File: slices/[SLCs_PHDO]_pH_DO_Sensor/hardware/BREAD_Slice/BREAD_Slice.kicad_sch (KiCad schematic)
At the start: 1 part, among them J8 Conn_01x10_Female

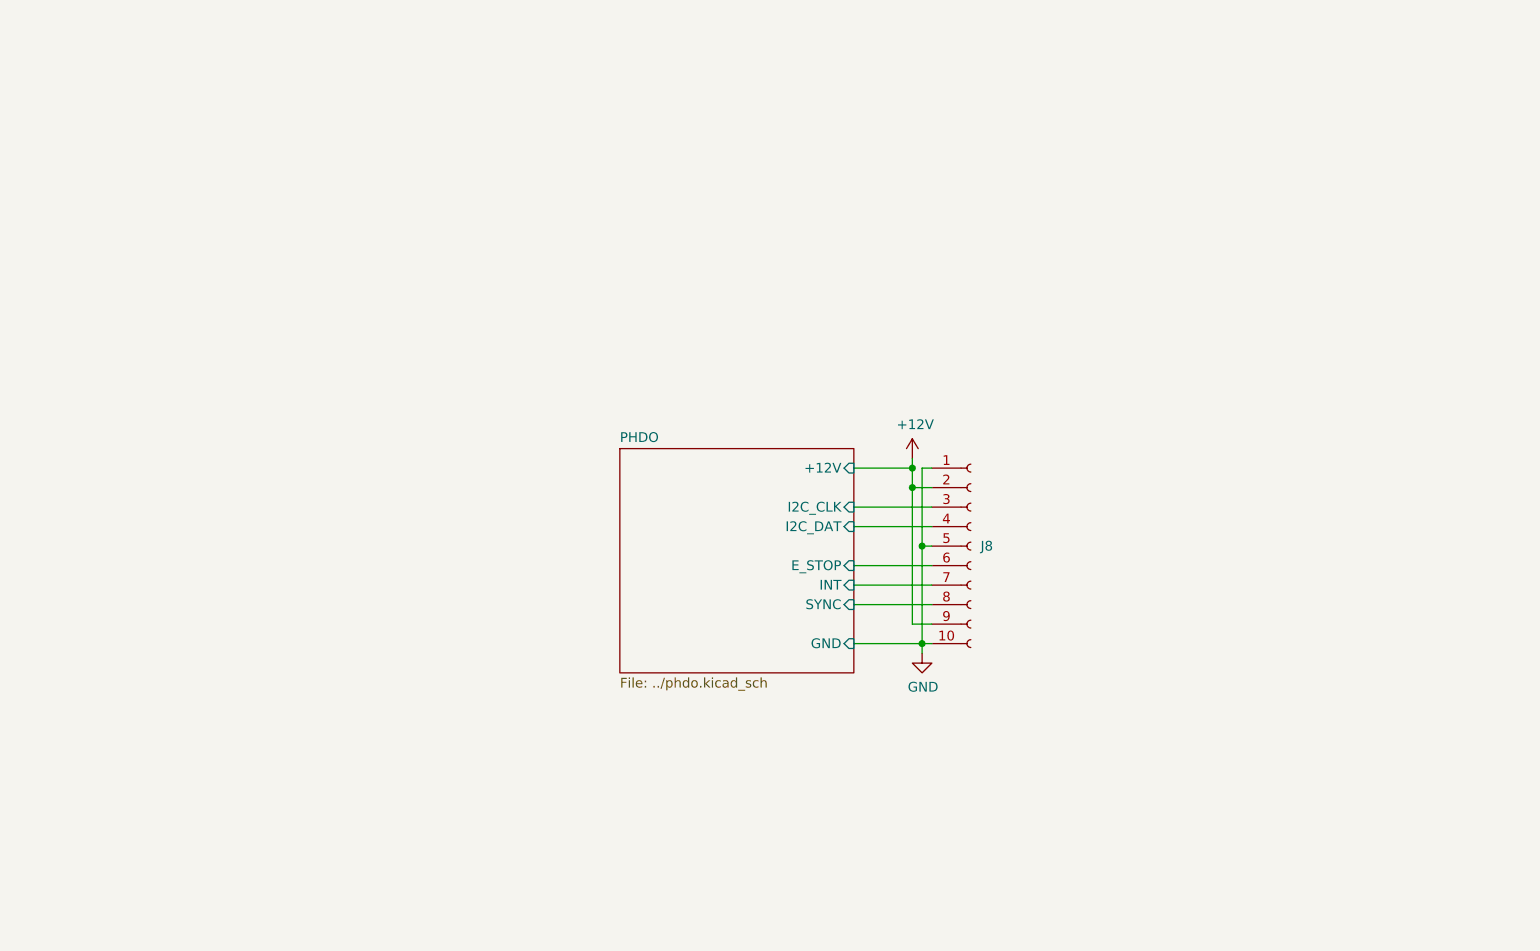
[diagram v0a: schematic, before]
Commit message: improved phdo and initial ERC pass on PDER
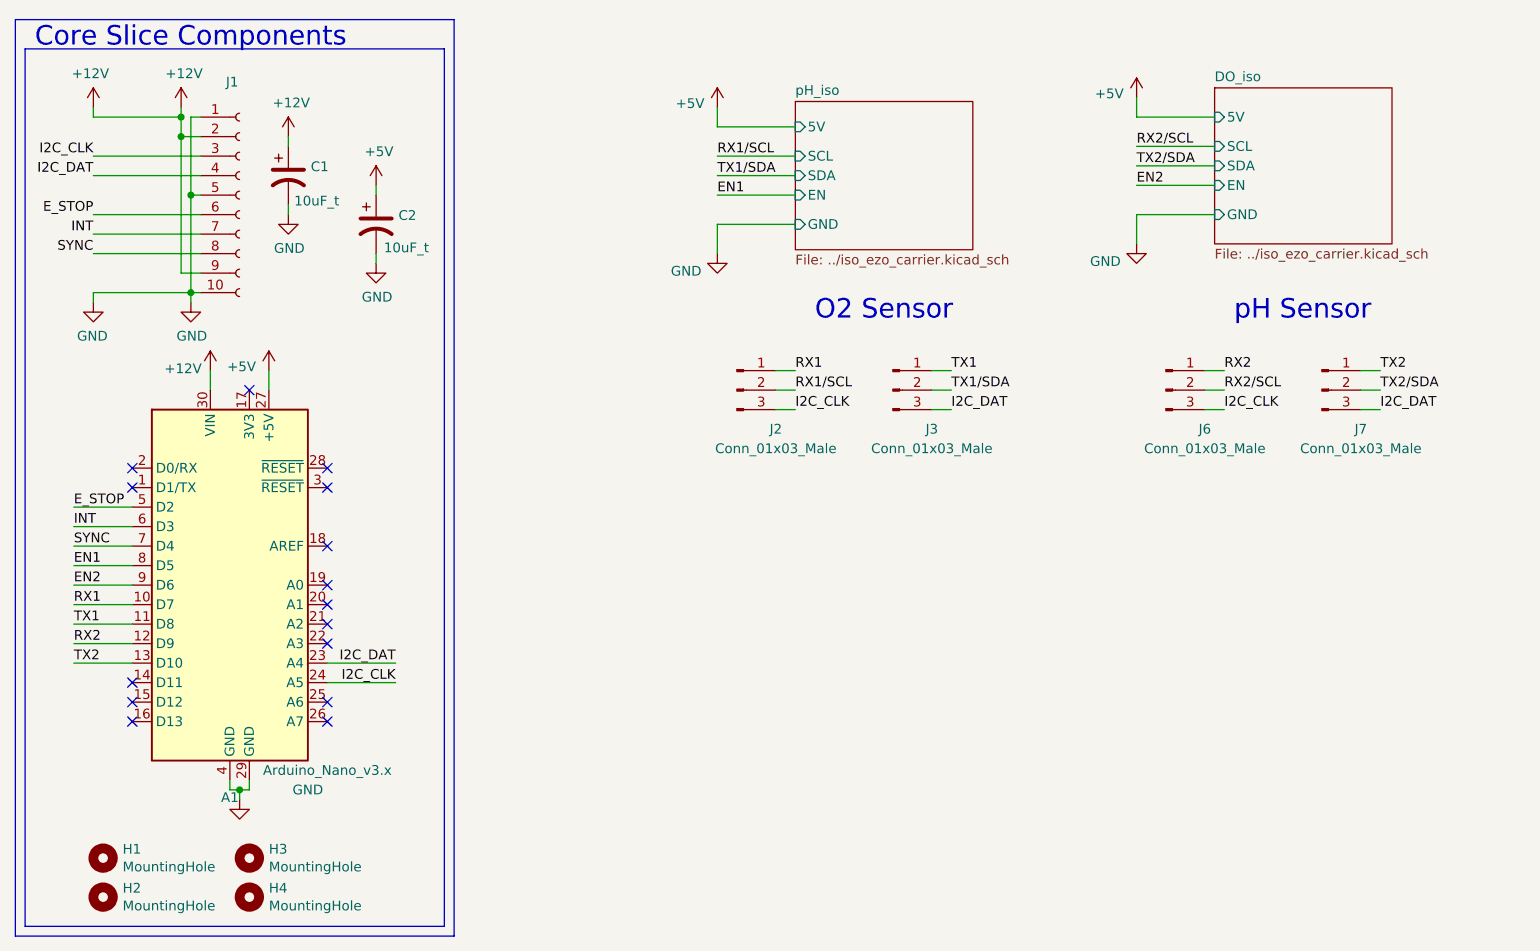
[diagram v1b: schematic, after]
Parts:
- removed J8: Conn_01x10_Female, Connector_PinSocket_2.54mm:PinSocket_1x10_P2.54mm_Horizontal, symbol Connector:Conn_01x10_Female
- added A1: Arduino_Nano_v3.x, Module:Arduino_Nano, symbol MCU_Module:Arduino_Nano_v3.x
- added C1, C2: 10uF_t, Extras:C_1206_3216Metric_Pad1.33x1.80mm_HandSolder, symbol BREAD_Slice-rescue:10uF_t-OCI_UPL_2_Capacitors
- added H1, H2, H3, H4: MountingHole, MountingHole:MountingHole_3.2mm_M3_DIN965_Pad, symbol Mechanical:MountingHole
- added J1: Conn_01x10_Female, Connector_PinSocket_2.54mm:PinSocket_1x10_P2.54mm_Horizontal, symbol Connector:Conn_01x10_Female
- added J2, J3, J6, J7: Conn_01x03_Male, Connector_PinSocket_2.54mm:PinSocket_1x03_P2.54mm_Vertical, symbol Connector:Conn_01x03_Male
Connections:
- net +12V: now also A1.30 (VIN), C1.1, J1.2 (Pin_2), J1.9 (Pin_9)
- net GND: now also A1.29 (GND), A1.4 (GND), C1.2, C2.2, J1.1 (Pin_1), J1.10 (Pin_10), J1.5 (Pin_5)
- new net +5V: A1.27 (+5V), C2.1
- new net EN1: A1.8 (D5)
- new net EN2: A1.9 (D6)
- new net E_STOP: A1.5 (D2), J1.6 (Pin_6)
- new net I2C_CLK: A1.24 (A5), J1.3 (Pin_3), J2.3 (Pin_3), J6.3 (Pin_3)
- new net I2C_DAT: A1.23 (A4), J1.4 (Pin_4), J3.3 (Pin_3), J7.3 (Pin_3)
- new net INT: A1.6 (D3), J1.7 (Pin_7)
- new net RX1: A1.10 (D7), J2.1 (Pin_1)
- new net RX1/SCL: J2.2 (Pin_2)
- new net RX2: A1.12 (D9), J6.1 (Pin_1)
- new net RX2/SCL: J6.2 (Pin_2)
- new net SYNC: A1.7 (D4), J1.8 (Pin_8)
- new net TX1: A1.11 (D8), J3.1 (Pin_1)
- new net TX1/SDA: J3.2 (Pin_2)
- new net TX2: A1.13 (D10), J7.1 (Pin_1)
- new net TX2/SDA: J7.2 (Pin_2)
- no-connect marks 0 -> 15
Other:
- removed sheet PHDO
- added sheet DO_iso (../iso_ezo_carrier.kicad_sch)
- added sheet pH_iso (../iso_ezo_carrier.kicad_sch)
- note added: "Core Slice Components"
- note added: "O2 Sensor"
- note added: "pH Sensor"
